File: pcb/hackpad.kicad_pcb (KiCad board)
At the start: 2 copper layers, 107.8 x 87 mm, 42 parts, among them J1 OLED DISPLAY, SW1 SW_Push, SW10 SW_Push, SW11 SW_Push, SW12 SW_Push, SW13 SW_Push, SW14 SW_Push, SW15 SW_Push, SW16 SW_Push, SW17 SW_Push, SW18 RotaryEncoder_Switch, SW2 SW_Push, SW3 SW_Push, SW4 RotaryEncoder_Switch, SW5 RotaryEncoder_Switch, SW6 SW_Push, SW7 SW_Push, SW8 SW_Push, SW9 SW_Push, U1 MOUDLE-SEEEDUINO-XIAO, U2 MCP23017_SO

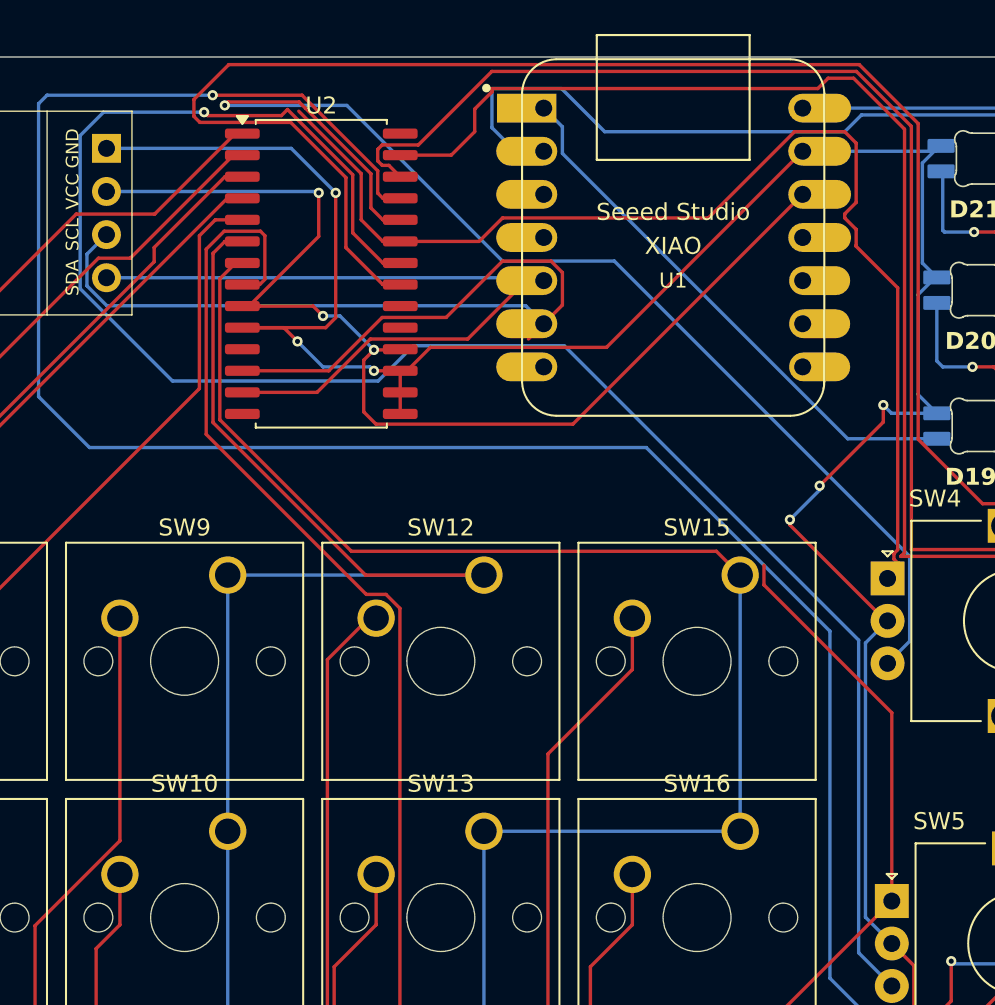
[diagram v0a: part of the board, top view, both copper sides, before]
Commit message: add bom and cleanup pcb
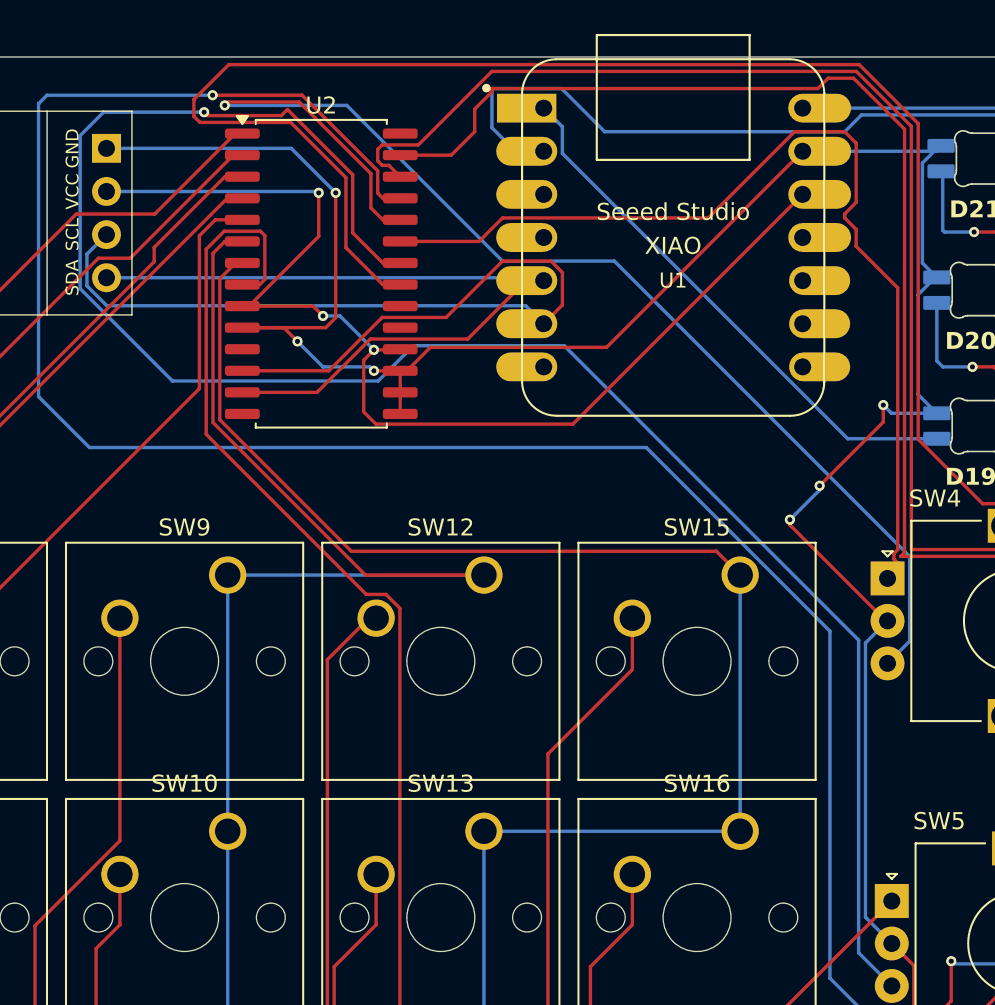
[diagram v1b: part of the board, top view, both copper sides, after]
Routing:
- net ROT1A: track 241.1 -> 218.2 mm
- net ROT2A: track 68.3 -> 57.6 mm
- net SCL: track 57.9 -> 56.6 mm
- net +3.3V: track 68.4 -> 67.3 mm
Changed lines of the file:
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@@
-	)
-	(segment
-		(start 136.25 52.21)
-		(end 135.351 53.109)
-		(width 0.2)
-		(layer "F.Cu")
-		(net 29)
 	)
 	(segment
@@
 		(start 122.67 51.17)
 		(end 123.25 51.75)
-		(width 0.2)
-		(layer "F.Cu")
-		(net 30)
-	)
-	(segment
-		(start 118.5 51.17)
-		(end 119.524999 51.17)
 		(width 0.2)
 		(layer "F.Cu")
@@
 	)
 	(segment
-		(start 125.5 46.084999)
-		(end 125.5 43.3658)
-		(width 0.2)
-		(layer "F.Cu")
-		(net 34)
-	)
-	(segment
 		(start 145.94324 45.979)
 		(end 151.02324 40.899)
@@
 	)
 	(segment
-		(start 125.5 43.3658)
-		(end 121.82465 39.69045)
-		(width 0.2)
-		(layer "F.Cu")
-		(net 34)
-	)
-	(segment
 		(start 127.8 47.36)
 		(end 132.44224 47.36)
@@
 	)
 	(segment
-		(start 127.8 47.36)
-		(end 126.775001 47.36)
-		(width 0.2)
-		(layer "F.Cu")
-		(net 34)
-	)
-	(segment
 		(start 154.651 45.06676)
 		(end 153.97676 45.741)
@@
 	)
 	(segment
-		(start 126.775001 47.36)
-		(end 125.5 46.084999)
-		(width 0.2)
-		(layer "F.Cu")
-		(net 34)
-	)
-	(segment
 		(start 156.5 67)
 		(end 156.5 67.21)
@@
 	)
 	(segment
-		(start 122.22565 39.52435)
-		(end 121.8523 39.151)
-		(width 0.2)
-		(layer "F.Cu")
-		(net 35)
-	)
-	(segment
-		(start 126.073 43.3717)
-		(end 122.22565 39.52435)
+		(start 121.8523 39.151)
+		(end 126.073 43.3717)
 		(width 0.2)
 		(layer "F.Cu")
@@
 	)
 	(segment
-		(start 149.221 67.590314)
-		(end 149.221 66.429686)
-		(width 0.2)
-		(layer "F.Cu")
-		(net 37)
-	)
-	(segment
 		(start 158.302 59.012)
 		(end 162.099 62.809)
@@
 	)
 	(segment
-		(start 156.75 86.21)
-		(end 156.75 75.119314)
-		(width 0.2)
-		(layer "F.Cu")
-		(net 37)
-	)
-	(segment
 		(start 142.929 106.00975)
 		(end 142.929 100.031)
-		(width 0.2)
-		(layer "F.Cu")
-		(net 37)
-	)
-	(segment
-		(start 156.75 75.119314)
-		(end 149.221 67.590314)
 		(width 0.2)
 		(layer "F.Cu")
@@
 	(segment
 		(start 110.328 39.75)
-		(end 116 39.75)
+		(end 116.25 39.75)
 		(width 0.2)
 		(layer "B.Cu")
@@
 		(width 0.2)
 		(layer "B.Cu")
-		(net 38)
-	)
-	(segment
-		(start 116 39.75)
-		(end 116.25 39.75)
-		(width 0.2)
-		(layer "B.Cu")
